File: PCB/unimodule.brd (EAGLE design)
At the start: 103 x 74.2 mm, 132 parts, among them IC1 TTGO_DISP, IC2 DS18D20, IC3 FAN3111E, IC4 FAN3111E, IC5 FAN3111E, K1 XY2500(5.0)-4PV, K100 JSM1-12V-5, K101 XY2500(5.0)-4PV, K102 JST-B02B-JWPF-SK-R, K103 JST-B04B-JWPF-SK-R, K104 JST-B08B-JWPF-SK-R, K105 JST-B03B-JWPF-SK-R, U1 MAX3485, U2 LMR62014XMFE/NOPB0

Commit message: Fix components height
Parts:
- D3: device diode:SOD323-W -> siliXcon-semiconductors:SOD123F
- OK1, OK2, OK3: device optocoupler:DIL06 -> siliXcon-ICs:DIL06
- moved R36 12.5 mm to (73.6, -16.8), flipped to the top, turned to 90 degrees
- moved R37 10.8 mm to (61.1, -19.5), flipped to the top
- moved R34 9.59 mm to (71.5, -19.8), flipped to the top
- moved R38 7.65 mm to (63.6, -16.8), flipped to the top, turned to 90 degrees
- moved R23 3.61 mm to (53.0, -7.50), turned to 180 degrees
- moved R33 3.32 mm to (68.5, -16.8), flipped to the top, turned to 90 degrees
- moved SJ100 2.86 mm to (105.0, -7.30), flipped to the bottom, turned to 0 degrees
- moved P2 2.60 mm to (21.1, -67.8)
- moved R31 2.02 mm to (66.3, -19.8), flipped to the top
- moved R21 0.92 mm to (50.4, -6.70)
- moved R35 0.64 mm to (74.1, -20.3)
- moved R32 0.50 mm to (63.7, -20.2)
- moved R29 0.40 mm to (68.9, -20.3)
- moved C21 0.20 mm to (55.8, -17.8)
- moved C17 0.10 mm to (52.8, -6.60)
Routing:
- net L_OUT_2: track 21.3 -> 17.5 mm, vias 4 -> 3
- net +3V3: track 232.4 -> 235.8 mm
- net ENC_2: track 19.7 -> 22.5 mm, vias 0 -> 1
- net L_OUT_3: track 16.5 -> 14.4 mm, vias 4 -> 3
- net A4: track 16.1 -> 17.6 mm
- net A3: track 38.3 -> 39.7 mm
- net L_FUSED: track 2.15 -> 1.10 mm
- net OUT_3_SIG: track 36.3 -> 35.6 mm
- net L_OUT_1: track 14.8 -> 14.1 mm
- net N$15: track 2.73 -> 2.08 mm
- net AIN_1: track 9.82 -> 10.4 mm
- net N$12: track 22.3 -> 21.9 mm, vias 2 -> 1
- net A1: track 34.5 -> 34.8 mm, vias 2 -> 3
- net A2: track 33.1 -> 33.0 mm, vias 4 -> 3
- net GND: vias 220 -> 258

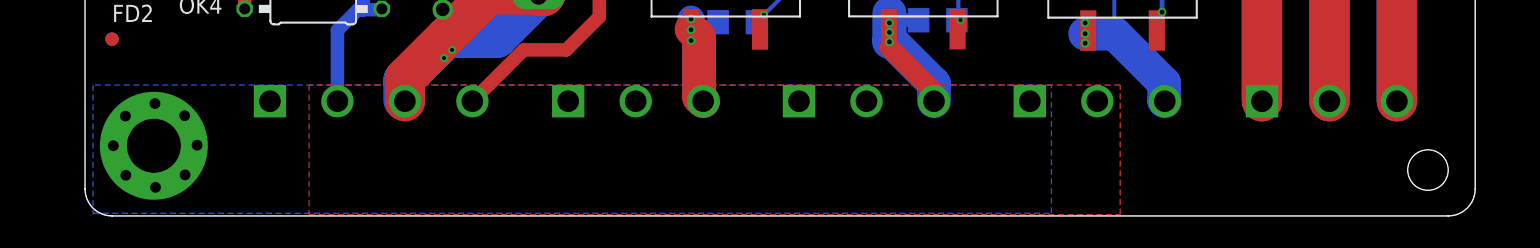
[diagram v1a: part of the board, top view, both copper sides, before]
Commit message: add connector description
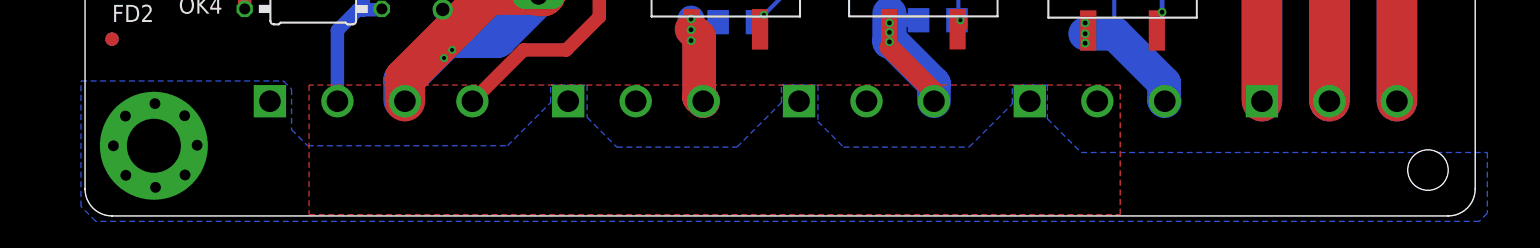
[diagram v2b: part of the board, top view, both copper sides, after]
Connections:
- net N$16 renamed R_NO
- net N$17 renamed R_C
- net N$18 renamed R_NC
- net N$22 renamed SDA_P
- net N$29 renamed SCL_P
- net N$30 renamed PWM_2
- net N$32 renamed PWM_1
- net N$35 renamed PWM_3
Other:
- board text added: "1"
- board text added: "2"
- board text added: "3"
- board text added: "3V 456"
- board text added: "3V3"
- board text added: "A1"
- board text added: "A2"
- board text added: "A3"
- board text added: "ENC"
- board text added: "G 321"
- board text added: "G IN 3V3"
- board text added: "GND"
- board text added: "L"
- board text added: "L_1"
- board text added: "L_2"
- board text added: "L_3"
- board text added: "N"
- board text added: "PE"
- board text added: "PWM OUT"
- board text added: "SCL"
- board text added: "SDA"
- board text added: "TEMP"
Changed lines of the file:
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@@
 <layer number="14" name="Route14" color="22" fill="1" visible="no" active="no"/>
 <layer number="15" name="Route15" color="23" fill="1" visible="no" active="no"/>
-<layer number="16" name="Bottom" color="1" fill="1" visible="yes" active="yes"/>
+<layer number="16" name="Bottom" color="1" fill="1" visible="no" active="yes"/>
 <layer number="17" name="Pads" color="2" fill="1" visible="yes" active="yes"/>
 <layer number="18" name="Vias" color="2" fill="1" visible="yes" active="yes"/>
@@
 <layer number="20" name="Dimension" color="24" fill="1" visible="yes" active="yes"/>
 <layer number="21" name="tPlace" color="7" fill="1" visible="yes" active="yes"/>
-<layer number="22" name="bPlace" color="7" fill="1" visible="yes" active="yes"/>
+<layer number="22" name="bPlace" color="7" fill="1" visible="no" active="yes"/>
 <layer number="23" name="tOrigins" color="15" fill="1" visible="yes" active="yes"/>
-<layer number="24" name="bOrigins" color="15" fill="1" visible="yes" active="yes"/>
+<layer number="24" name="bOrigins" color="15" fill="1" visible="no" active="yes"/>
 <layer number="25" name="tNames" color="7" fill="1" visible="no" active="yes"/>
 <layer number="26" name="bNames" color="7" fill="1" visible="no" active="yes"/>
@@
 <layer number="28" name="bValues" color="7" fill="1" visible="no" active="yes"/>
 <layer number="29" name="tStop" color="2" fill="3" visible="yes" active="yes"/>
-<layer number="30" name="bStop" color="2" fill="6" visible="yes" active="yes"/>
+<layer number="30" name="bStop" color="2" fill="6" visible="no" active="yes"/>
 <layer number="31" name="tCream" color="7" fill="4" visible="no" active="yes"/>
 <layer number="32" name="bCream" color="7" fill="5" visible="no" active="yes"/>
@@
 <layer number="40" name="bKeepout" color="1" fill="11" visible="no" active="yes"/>
 <layer number="41" name="tRestrict" color="4" fill="10" visible="yes" active="yes"/>
-<layer number="42" name="bRestrict" color="1" fill="10" visible="yes" active="yes"/>
+<layer number="42" name="bRestrict" color="1" fill="10" visible="no" active="yes"/>
 <layer number="43" name="vRestrict" color="2" fill="10" visible="yes" active="yes"/>
 <layer number="44" name="Drills" color="7" fill="1" visible="no" active="yes"/>
@@
 <layer number="50" name="dxf" color="7" fill="1" visible="no" active="no"/>
 <layer number="51" name="tDocu" color="7" fill="1" visible="yes" active="yes"/>
-<layer number="52" name="bDocu" color="7" fill="1" visible="yes" active="yes"/>
+<layer number="52" name="bDocu" color="7" fill="1" visible="no" active="yes"/>
 <layer number="53" name="tGND_GNDA" color="7" fill="1" visible="no" active="no"/>
 <layer number="54" name="bGND_GNDA" color="7" fill="1" visible="no" active="no"/>
@@
 <rectangle x1="33.3" y1="-71" x2="36" y2="-63.3" layer="29"/>
 <rectangle x1="36" y1="-71" x2="87.6" y2="-68.5" layer="29"/>
-<text x="117.4" y="-34.2" size="1.778" layer="30" rot="MR0">Matous Cmelik 2020</text>
+<text x="92.5" y="-38.2" size="1.778" layer="30" rot="MR0">Matous Cmelik 2020</text>
 <text x="22.2" y="-22.5" size="1.778" layer="29" rot="R90">rev_1a</text>
 <text x="19.5" y="-26.4" size="1.778" layer="29" rot="R90">ESP32_unimodule</text>
 <text x="17.5" y="-29.2" size="1.778" layer="30" rot="MR90">github.com/cmeldas</text>
+<text x="31.2" y="-71.5" size="1.778" layer="30" rot="MR0">PE</text>
+<text x="35.5" y="-71.5" size="1.778" layer="30" rot="MR0">N</text>
+<text x="40.2" y="-71.5" size="1.778" layer="30" rot="MR0">L</text>
+<text x="53.1" y="-71.6" size="1.778" layer="30" rot="MR0">PE</text>
+<text x="57.3" y="-71.6" size="1.778" layer="30" rot="MR0">N</text>
+<text x="74.7" y="-71.6" size="1.778" layer="30" rot="MR0">N</text>
+<text x="91.8" y="-71.6" size="1.778" layer="30" rot="MR0">N</text>
+<text x="70.3" y="-71.6" size="1.778" layer="30" rot="MR0">PE</text>
+<text x="87.2" y="-71.6" size="1.778" layer="30" rot="MR0">PE</text>
+<text x="63.7" y="-71.6" size="1.778" layer="30" rot="MR0">L_1</text>
+<text x="98" y="-71.5" size="1.778" layer="30" rot="MR0">L_3</text>
+<text x="81" y="-71.6" size="1.778" layer="30" rot="MR0">L_2</text>
+<wire x1="103" y1="-68.4" x2="103" y2="-70.6" width="0.3" layer="30"/>
+<wire x1="112.4" y1="-68.3" x2="112.4" y2="-70.5" width="0.3" layer="30"/>
+<wire x1="107.7" y1="-68.5" x2="107.7" y2="-69.5" width="0.3" layer="30"/>
+<wire x1="107.7" y1="-69.5" x2="103.1" y2="-71.5" width="0.3" layer="30"/>
+<text x="110.3" y="-34.4" size="1.778" layer="30" rot="MR0">1</text>
+<text x="105.4" y="-34.4" size="1.778" layer="30" rot="MR0">2</text>
+<text x="100" y="-34.4" size="1.778" layer="30" rot="MR0">3</text>
+<text x="117.2" y="-34.4" size="1.778" layer="30" rot="MR0">GND</text>
+<text x="98.9" y="-21.2" size="1.016" layer="30" rot="MR0">PWM OUT</text>
+<text x="79.7" y="-7.3" size="1.27" layer="30" rot="MR0">SDA</text>
+<text x="79.7" y="-9.2" size="1.27" layer="30" rot="MR0">3V3</text>
+<text x="79.7" y="-5.4" size="1.27" layer="30" rot="MR0">SCL</text>
+<text x="95.2" y="-11.5" size="1.27" layer="30" rot="MR0">ENC</text>
+<text x="64.3" y="-11.2" size="1.27" layer="30" rot="MR0">A1</text>
+<text x="67.7" y="-11.2" size="1.27" layer="30" rot="MR0">A2</text>
+<text x="72.1" y="-11.3" size="1.27" layer="30" rot="MR0">A3</text>
+<text x="78.1" y="-11.3" size="1.27" layer="30" rot="MR0">GND</text>
+<text x="47" y="-8.1" size="1.27" layer="30" rot="MR0">G 321</text>
+<text x="55" y="-21.1" size="1.27" layer="30" rot="MR0">3V 456</text>
+<text x="32.6" y="-4" size="1.016" layer="30" rot="MR270">TEMP</text>
+<text x="34.1" y="-0.7" size="1.016" layer="30" rot="MR180">G  IN  3V3</text>
+<text x="89.8" y="-70.6" size="1.778" layer="29">N</text>
 </plain>
 <attributes>
@@
 <wire x1="105.8" y1="-9.1" x2="105.6" y2="-9.3" width="0.3" layer="16"/>
 </signal>
-<signal name="N$16" class="1">
+<signal name="R_NO" class="1">
 <contactref element="U$100" pad="P$3"/>
 <contactref element="K100" pad="3"/>
@@
 <wire x1="113.2" y1="-55.4" x2="113.2" y2="-64.5" width="3" layer="1"/>
 </signal>
-<signal name="N$17" class="1">
+<signal name="R_C" class="1">
 <contactref element="K100" pad="1"/>
 <contactref element="U$100" pad="P$2"/>
@@
 <wire x1="108.2" y1="-40.2" x2="108.3" y2="-40.1" width="3" layer="1"/>
 </signal>
-<signal name="N$18">
+<signal name="R_NC">
 <contactref element="U$100" pad="P$1"/>
 <contactref element="K100" pad="4"/>
@@
 </signal>
 <signal name="PE" class="1">
-<polygon width="0.1016" layer="16" thermals="no">
-<vertex x="16.6" y="-63.3"/>
-<vertex x="16.6" y="-72.8"/>
-<vertex x="87.6" y="-72.8"/>
-<vertex x="87.6" y="-63.3"/>
-</polygon>
 <contactref element="U$104" pad="P$1"/>
 <contactref element="U$103" pad="P$1"/>
@@
 <contactref element="P2" pad="P$5" route="any" routetag="G$1.P"/>
 <contactref element="P2" pad="P$9" route="any" routetag="G$1.P"/>
+<polygon width="0.3" layer="16" thermals="no">
+<vertex x="15.7" y="-63"/>
+<vertex x="30.7" y="-63"/>
+<vertex x="31.3" y="-63.6"/>
+<vertex x="31.3" y="-66.6"/>
+<vertex x="32.5" y="-67.8"/>
+<vertex x="47.3" y="-67.8"/>
+<vertex x="50.5" y="-64.6"/>
+<vertex x="50.5" y="-63.3"/>
+<vertex x="53.2" y="-63.3"/>
+<vertex x="53.2" y="-65.7"/>
+<vertex x="55.4" y="-67.9"/>
+<vertex x="64.3" y="-67.9"/>
+<vertex x="67.6" y="-64.6"/>
+<vertex x="67.6" y="-63.3"/>
+<vertex x="70.3" y="-63.3"/>
+<vertex x="70.3" y="-66"/>
+<vertex x="72.2" y="-67.9"/>
+<vertex x="81.5" y="-67.9"/>
+<vertex x="84.7" y="-64.7"/>
+<vertex x="84.7" y="-63.3"/>
+<vertex x="87.3" y="-63.3"/>
+<vertex x="87.3" y="-65.8"/>
+<vertex x="89.8" y="-68.3"/>
+<vertex x="119.9" y="-68.3"/>
+<vertex x="119.9" y="-72.8"/>
+<vertex x="119.3" y="-73.4"/>
+<vertex x="16.8" y="-73.4"/>
+<vertex x="15.7" y="-72.3"/>
+</polygon>
 </signal>
 <signal name="N$20">
@@
 <wire x1="63.1" y1="-20.45" x2="62.85" y2="-20.2" width="0.3" layer="1"/>
 </signal>
-<signal name="N$22">
+<signal name="SDA_P">
 <contactref element="K103" pad="3"/>
 <contactref element="R8" pad="2"/>
@@
 <wire x1="80.9" y1="-6.95" x2="80.25" y2="-7.6" width="0.3" layer="1"/>
 </signal>
-<signal name="N$29">
+<signal name="SCL_P">
 <contactref element="R13" pad="2"/>
 <contactref element="K103" pad="2"/>
@@
 <wire x1="112.828" y1="-18.91210625" x2="112.26589375" y2="-18.35" width="0.5" layer="16"/>
 </signal>
-<signal name="N$32">
+<signal name="PWM_1">
 <contactref element="R14" pad="2"/>
 <contactref element="K101" pad="P$2"/>
@@
 <wire x1="106.95" y1="-18.528" x2="106.95" y2="-18.35" width="0.5" layer="16"/>
 </signal>
-<signal name="N$30">
+<signal name="PWM_2">
 <contactref element="R17" pad="2"/>
 <contactref element="K101" pad="P$3"/>
@@
 <wire x1="102.2" y1="-18.4" x2="102.2" y2="-19.178" width="0.5" layer="16"/>
 </signal>
-<signal name="N$35">
+<signal name="PWM_3">
 <contactref element="R18" pad="2"/>
 <contactref element="K101" pad="P$4"/>

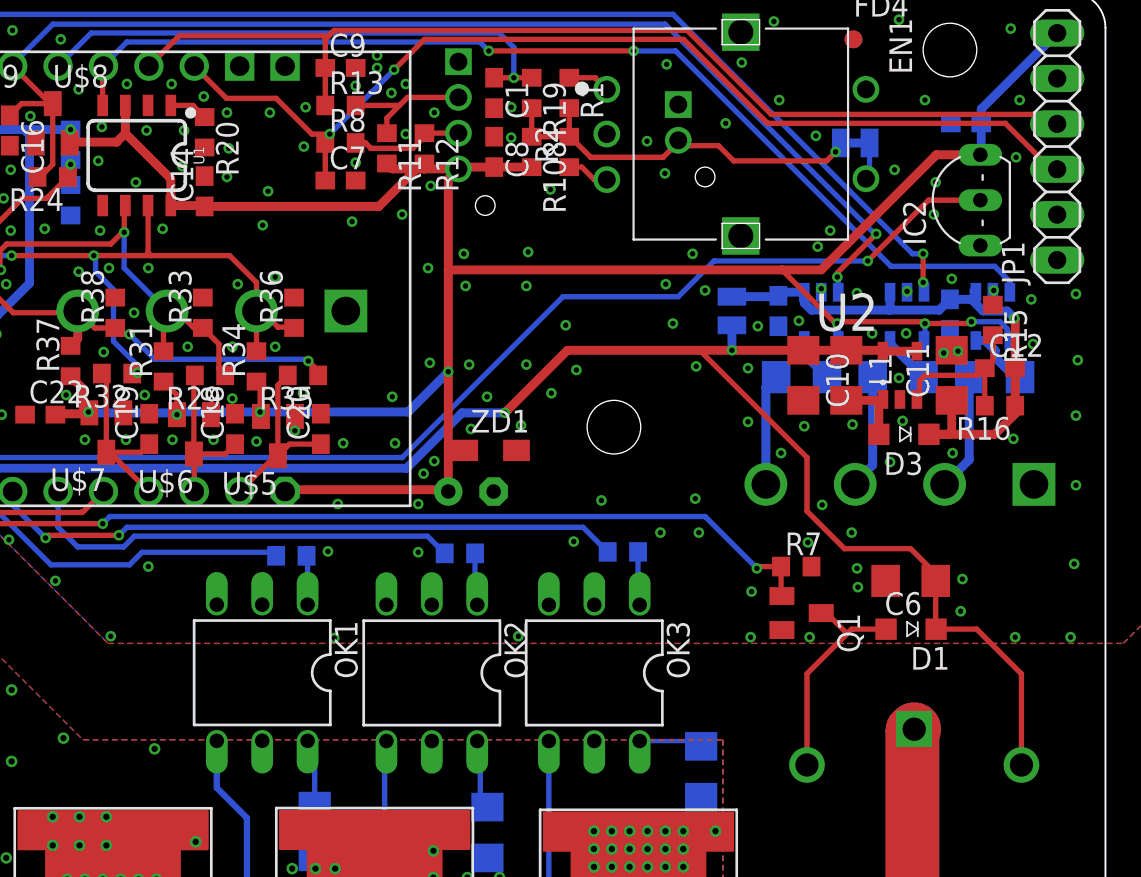
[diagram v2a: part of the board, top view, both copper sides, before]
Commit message: add status LEDs
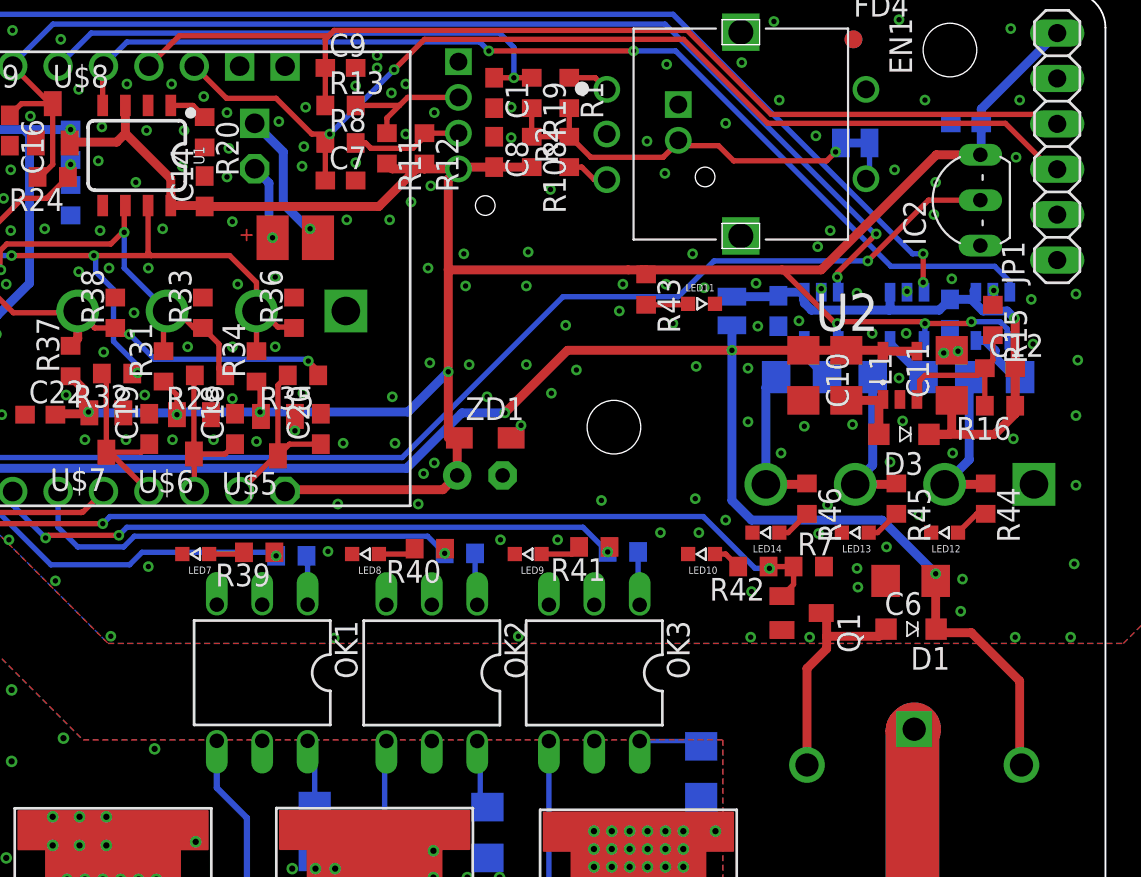
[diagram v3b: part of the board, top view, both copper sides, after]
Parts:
- added C26: DISP_BATSMD, TTGO_LCD_DISP:BAT_SMD
- added C27: DISP_BAT2,54, TTGO_LCD_DISP:BAT_THT_254
- added LED10, LED11, LED12, LED13, LED14, LED7, LED8, LED9: (no value), siliXcon-semiconductors:LED-0603
- added R39, R40, R41, R42, R43: 220R, rcl:R0603
- added R44, R45, R46: 1k, rcl:R0603
- C100: value 220uF / 6.3V -> 330uF / 6.3V; device rcl:E2,5-6 -> rcl:E2,5-7
- C101: value 220uF / 6.3V -> 330uF / 6.3V
- K100: value JSM1-12V-5 -> G5LE-1-E 5VDC OMRON
- moved C100 1.03 mm to (84.0, -25.9)
- moved ZD1 0.76 mm to (84.3, -23.8)
- moved R7 0.70 mm to (102.4, -31.0)
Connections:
- new net BAT+: C26.BAT+, C27.BAT+
- new net BAT-: C26.BAT-, C27.BAT-
- new net N$16: LED7.A, R39.2
- new net N$17: LED8.A, R40.2
- new net N$18: LED9.A, R41.2
- new net N$21: LED10.A, R42.2
- new net N$22: LED11.A, R43.2
- new net N$29: LED12.A, R44.2
- new net N$30: LED13.A, R45.2
- new net N$32: LED14.A, R46.2
- net +3V3: now also R43.1
- net GND: now also LED10.C, LED11.C, LED12.C, LED13.C, LED14.C, LED7.C, LED8.C, LED9.C
- net OUT_1_SIG: now also R39.1
- net OUT_2_SIG: now also R40.1
- net OUT_3_SIG: now also R41.1
- net PWM_1: now also R44.1
- net PWM_2: now also R45.1
- net PWM_3: now also R46.1
- net RELAY_SIG: now also R42.1
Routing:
- net BAT-: track 0.00 -> 7.92 mm, vias 0 -> 1
- net BAT+: track 0.00 -> 5.72 mm, vias 0 -> 1
- net N$22: track 0.00 -> 2.37 mm
- net PWM_3: track 6.24 -> 8.56 mm
- net PWM_2: track 6.41 -> 8.73 mm
- net PWM_1: track 6.57 -> 8.89 mm
- net N$18: track 0.00 -> 2.27 mm
- net N$17: track 0.00 -> 2.12 mm
- net N$16: track 0.00 -> 1.99 mm
- net N$32: track 0.00 -> 1.98 mm
- net N$30: track 0.00 -> 1.98 mm
- net N$29: track 0.00 -> 1.98 mm
- net N$21: track 0.00 -> 1.59 mm
- net RELAY_SIG: track 55.0 -> 56.1 mm
- net +5V: track 168.4 -> 169.5 mm, vias 8 -> 9
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
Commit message: some minor changes, tweaks
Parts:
- moved R39 75.4 mm to (55.9, 43.5)
- moved R9 75.3 mm to (17.1, 15.9)
- moved C1 75.2 mm to (69.0, 69.0)
- moved C10 75.2 mm to (86.3, 53.2)
- moved C100 75.2 mm to (68.2, 47.6)
- moved C101 75.2 mm to (30.5, 50.8)
- moved C11 75.2 mm to (94.6, 53.2)
- moved C12 75.2 mm to (97.3, 53.6)
- moved C13 75.2 mm to (94.5, 56.6)
- moved C14 75.2 mm to (52.8, 63.5)
- moved C15 75.2 mm to (31.8, 66.9)
- moved C16 75.2 mm to (41.9, 66.9)
- moved C17 75.2 mm to (37.0, 66.9)
- moved C18 75.2 mm to (54.5, 50.2)
- moved C19 75.2 mm to (49.7, 50.2)
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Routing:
- net L_IN: track 82.5 -> 90.9 mm, vias 4 -> 11
- net L_OUT_3: track 14.4 -> 17.6 mm, vias 3 -> 6
- net L_OUT_1: track 14.1 -> 17.2 mm, vias 3 -> 6
- net N$12: track 21.9 -> 23.5 mm, vias 1 -> 2
- net N$6: track 24.3 -> 25.5 mm, vias 1 -> 2
- net N$9: track 19.6 -> 20.4 mm, vias 1 -> 2
- net N$7: track 3.93 -> 4.50 mm
- net L_OUT_2: track 17.5 -> 17.7 mm, vias 3 -> 6
- net L_FUSED: vias 117 -> 125
- net GND: vias 263 -> 265
